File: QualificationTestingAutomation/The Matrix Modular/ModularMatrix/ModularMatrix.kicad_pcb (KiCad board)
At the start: 4 copper layers, 92.7 x 116.8 mm, 82 parts, among them J1 Conn_02x32_Counter_Clockwise_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, J2 Raspberry_Pi_2_3, J3 Barrel_Jack_MountingPin, J5 Conn_02x32_Counter_Clockwise_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, J6 Banana Jack, J7 Banana Jack, J8 Banana Jack, J9 Banana Jack, U1 TPS563210, U2 LT8361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

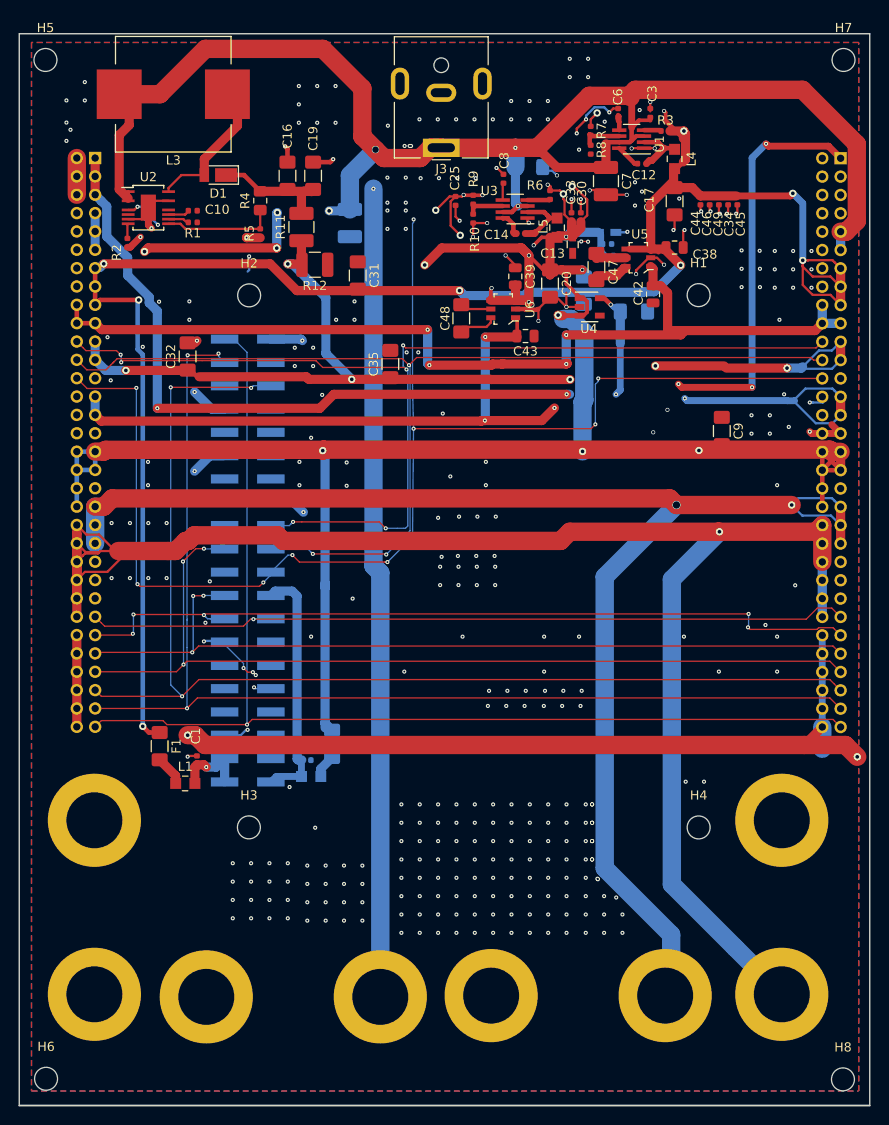
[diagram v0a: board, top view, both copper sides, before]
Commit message: Cleaned up the libraries Cleaned up the tracks Adjusted footprints to the manufacturers minimum size.
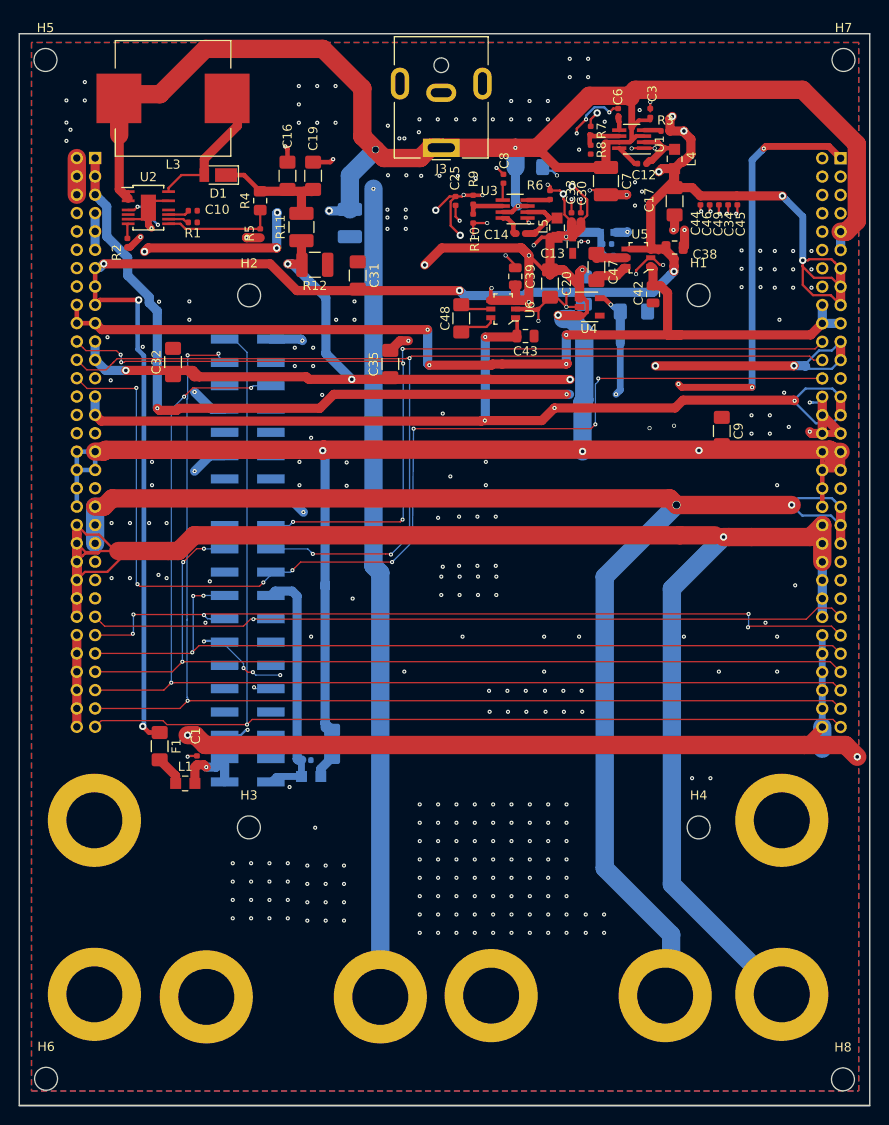
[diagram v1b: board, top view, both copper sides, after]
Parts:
- moved C32 1.70 mm to (178.0, 90.7)
- moved L3 0.46 mm to (178.0, 62.0)
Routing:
- net MOSI0: track 146.0 -> 122.8 mm, vias 9 -> 8
- net VD: track 223.1 -> 202.8 mm
- net SCLK1: track 128.0 -> 123.6 mm
- net GND: track 115.9 -> 119.3 mm, vias 346 -> 310
- net SCLK0: track 119.3 -> 116.5 mm
- net +5V: track 198.9 -> 196.4 mm, vias 10 -> 11
- net HT: track 115.0 -> 117.3 mm
- net +12V: track 202.3 -> 201.1 mm
- net MOSI1: track 125.5 -> 124.4 mm
- net -3V3: track 109.9 -> 108.9 mm
- net MISO0: track 117.8 -> 118.5 mm
- net +1V8: track 149.6 -> 149.0 mm

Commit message: Added Voltage and current measurment of the muxes and relays to the MSP Some clean up of the tracks.
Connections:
- J1 pad 49: GND -> VD
- J5 pad 49: GND -> VD
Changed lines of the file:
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@@
   )
   (setup
-    (last_trace_width 0.125)
+    (last_trace_width 0.0889)
     (user_trace_width 0.09)
     (user_trace_width 0.125)
@@
       (net 34 VD))
     (pad 49 thru_hole oval (at 0 -48 180) (size 1.35 1.35) (drill 0.8) (layers *.Cu *.Mask)
-      (net 1 GND))
+      (net 34 VD))
     (pad 48 thru_hole oval (at 2 -46 180) (size 1.35 1.35) (drill 0.8) (layers *.Cu *.Mask)
       (net 34 VD))
@@
       (net 34 VD))
     (pad 49 thru_hole oval (at 0 -48 180) (size 1.35 1.35) (drill 0.8) (layers *.Cu *.Mask)
-      (net 1 GND))
+      (net 34 VD))
     (pad 48 thru_hole oval (at 2 -46 180) (size 1.35 1.35) (drill 0.8) (layers *.Cu *.Mask)
       (net 34 VD))
@@
   (via (at 232.8672 106.299) (size 0.9) (drill 0.8) (layers F.Cu B.Cu) (net 33))
   (segment (start 233.0705 106.5023) (end 232.8672 106.299) (width 1) (layer F.Cu) (net 33))
-  (segment (start 188.707 118.51894) (end 188.707 118.383731) (width 0.09) (layer B.Cu) (net 37) (status 30))
-  (segment (start 183.6112 118.7018) (end 181.9862 118.7018) (width 0.125) (layer B.Cu) (net 38) (status 10))
-  (via (at 181.3052 116.1923) (size 0.45) (drill 0.2) (layers F.Cu B.Cu) (net 39))
-  (segment (start 183.6112 116.1618) (end 181.3357 116.1618) (width 0.125) (layer B.Cu) (net 39) (status 10))
-  (segment (start 181.3357 116.1618) (end 181.3052 116.1923) (width 0.125) (layer B.Cu) (net 39))
-  (via (at 180.1876 116.2177) (size 0.45) (drill 0.2) (layers F.Cu B.Cu) (net 39))
-  (segment (start 181.3052 116.1923) (end 180.213 116.1923) (width 0.125) (layer F.Cu) (net 39))
-  (segment (start 180.213 116.1923) (end 180.1876 116.2177) (width 0.125) (layer F.Cu) (net 39))
-  (segment (start 183.657 110.89894) (end 183.16956 110.89894) (width 0.5) (layer B.Cu) (net 40) (status 30))
-  (segment (start 183.6112 111.0818) (end 182.6112 111.0818) (width 0.125) (layer B.Cu) (net 40) (status 30))
-  (segment (start 183.657 105.81894) (end 183.20045 105.81894) (width 0.5) (layer B.Cu) (net 53) (status 30))
-  (segment (start 183.657 105.81894) (end 182.582 105.81894) (width 0.25) (layer B.Cu) (net 53) (status 30))
-  (segment (start 226.629065 64.537225) (end 226.455065 64.363225) (width 0.25) (layer F.Cu) (net 62))
-  (segment (start 226.629065 65.438225) (end 226.629065 64.537225) (width 0.25) (layer F.Cu) (net 62) (status 10))
-  (segment (start 226.5045 64.31379) (end 226.5045 63.7945) (width 0.0889) (layer F.Cu) (net 62) (status 30))
-  (segment (start 226.455065 64.363225) (end 226.5045 64.31379) (width 0.0889) (layer F.Cu) (net 62) (status 20))
-  (segment (start 226.5045 64.41266) (end 226.5045 64.1895) (width 0.5) (layer F.Cu) (net 62) (status 20))
-  (segment (start 226.629065 64.537225) (end 226.5045 64.41266) (width 0.5) (layer F.Cu) (net 62))
-  (segment (start 226.629065 63.919065) (end 226.5045 63.7945) (width 0.5) (layer F.Cu) (net 62) (status 30))
-  (segment (start 226.629065 65.438225) (end 226.629065 63.919065) (width 0.5) (layer F.Cu) (net 62) (status 30))
-  (segment (start 213.929065 71.301225) (end 214.009065 71.221225) (width 0.25) (layer F.Cu) (net 63) (status 30))
-  (segment (start 213.929065 73.058225) (end 213.929065 71.301225) (width 0.25) (layer F.Cu) (net 63) (status 30))
-  (segment (start 228.31884 69.088) (end 226.629065 67.398225) (width 0.5) (layer F.Cu) (net 64) (status 20))
-  (segment (start 228.623 69.088) (end 228.31884 69.088) (width 0.5) (layer F.Cu) (net 64) (status 10))
-  (segment (start 215.087065 75.695225) (end 214.438065 75.046225) (width 0.5) (layer F.Cu) (net 65) (status 20))
-  (segment (start 215.087065 76.570225) (end 215.087065 75.695225) (width 0.5) (layer F.Cu) (net 65))
-  (segment (start 213.957065 75.046225) (end 213.929065 75.018225) (width 0.5) (layer F.Cu) (net 65) (status 30))
-  (segment (start 214.438065 75.046225) (end 213.957065 75.046225) (width 0.5) (layer F.Cu) (net 65) (status 30))
-  (segment (start 215.22484 76.708) (end 215.087065 76.570225) (width 0.75) (layer F.Cu) (net 65) (status 10))
-  (segment (start 215.415 76.708) (end 215.22484 76.708) (width 0.75) (layer F.Cu) (net 65) (status 30))
   (via (at 245.4275 106.299) (size 0.8) (drill 0.4) (layers F.Cu B.Cu) (net 33))
   (segment (start 232.8672 106.299) (end 245.4275 106.299) (width 2) (layer F.Cu) (net 33))
@@
   (segment (start 251.2863 132.461) (end 252.575437 133.750137) (width 2) (layer F.Cu) (net 36))
   (segment (start 248.7615 130.5023) (end 248.7615 132.874) (width 2) (layer B.Cu) (net 36))
+  (segment (start 188.707 118.51894) (end 188.707 118.383731) (width 0.09) (layer B.Cu) (net 37) (status 30))
   (via (at 186.7535 118.745) (size 0.45) (drill 0.2) (layers F.Cu B.Cu) (net 37))
   (segment (start 188.6512 118.7018) (end 186.7967 118.7018) (width 0.125) (layer B.Cu) (net 37))
@@
   (segment (start 186.7535 118.745) (end 247.015 118.745) (width 0.125) (layer F.Cu) (net 37))
   (segment (start 247.015 118.745) (end 248.2215 117.5385) (width 0.125) (layer F.Cu) (net 37))
+  (segment (start 183.6112 118.7018) (end 181.9862 118.7018) (width 0.125) (layer B.Cu) (net 38) (status 10))
   (via (at 173.6725 118.237) (size 0.45) (drill 0.2) (layers F.Cu B.Cu) (net 38))
   (via (at 173.609 120.3325) (size 0.45) (drill 0.2) (layers F.Cu B.Cu) (net 38))
@@
   (segment (start 240.792 119.507) (end 249.7662 119.507) (width 0.125) (layer F.Cu) (net 38))
   (segment (start 240.665 119.634) (end 240.792 119.507) (width 0.125) (layer F.Cu) (net 38))
+  (via (at 181.3052 116.1923) (size 0.45) (drill 0.2) (layers F.Cu B.Cu) (net 39))
+  (segment (start 183.6112 116.1618) (end 181.3357 116.1618) (width 0.125) (layer B.Cu) (net 39) (status 10))
+  (segment (start 181.3357 116.1618) (end 181.3052 116.1923) (width 0.125) (layer B.Cu) (net 39))
+  (via (at 180.1876 116.2177) (size 0.45) (drill 0.2) (layers F.Cu B.Cu) (net 39))
+  (segment (start 181.3052 116.1923) (end 180.213 116.1923) (width 0.125) (layer F.Cu) (net 39))
+  (segment (start 180.213 116.1923) (end 180.1876 116.2177) (width 0.125) (layer F.Cu) (net 39))
   (via (at 180.086002 122.364498) (size 0.45) (drill 0.2) (layers F.Cu B.Cu) (net 39))
   (segment (start 180.1876 122.2629) (end 180.086002 122.364498) (width 0.125) (layer B.Cu) (net 39))
@@
   (segment (start 250.7615 122.5023) (end 249.890705 121.631505) (width 0.125) (layer F.Cu) (net 39))
   (segment (start 180.1876 116.2177) (end 180.1876 122.2629) (width 0.125) (layer B.Cu) (net 39))
+  (segment (start 183.657 110.89894) (end 183.16956 110.89894) (width 0.5) (layer B.Cu) (net 40) (status 30))
+  (segment (start 183.6112 111.0818) (end 182.6112 111.0818) (width 0.125) (layer B.Cu) (net 40) (status 30))
   (via (at 181.356 111.0615) (size 0.45) (drill 0.2) (layers F.Cu B.Cu) (net 40))
   (segment (start 183.6112 111.0818) (end 181.3763 111.0818) (width 0.125) (layer B.Cu) (net 40))
@@
   (segment (start 201.7395 111.6965) (end 201.67601 111.63301) (width 0.125) (layer F.Cu) (net 43))
   (segment (start 201.67601 111.63301) (end 201.16799 111.63301) (width 0.125) (layer F.Cu) (net 43))
+  (segment (start 183.657 105.81894) (end 183.20045 105.81894) (width 0.5) (layer B.Cu) (net 53) (status 30))
+  (segment (start 183.657 105.81894) (end 182.582 105.81894) (width 0.25) (layer B.Cu) (net 53) (status 30))
+  (segment (start 226.629065 64.537225) (end 226.455065 64.363225) (width 0.25) (layer F.Cu) (net 62))
+  (segment (start 226.629065 65.438225) (end 226.629065 64.537225) (width 0.25) (layer F.Cu) (net 62) (status 10))
+  (segment (start 226.5045 64.31379) (end 226.5045 63.7945) (width 0.0889) (layer F.Cu) (net 62) (status 30))
+  (segment (start 226.455065 64.363225) (end 226.5045 64.31379) (width 0.0889) (layer F.Cu) (net 62) (status 20))
+  (segment (start 226.5045 64.41266) (end 226.5045 64.1895) (width 0.5) (layer F.Cu) (net 62) (status 20))
+  (segment (start 226.629065 64.537225) (end 226.5045 64.41266) (width 0.5) (layer F.Cu) (net 62))
+  (segment (start 226.629065 63.919065) (end 226.5045 63.7945) (width 0.5) (layer F.Cu) (net 62) (status 30))
+  (segment (start 226.629065 65.438225) (end 226.629065 63.919065) (width 0.5) (layer F.Cu) (net 62) (status 30))
+  (segment (start 213.929065 71.301225) (end 214.009065 71.221225) (width 0.25) (layer F.Cu) (net 63) (status 30))
+  (segment (start 213.929065 73.058225) (end 213.929065 71.301225) (width 0.25) (layer F.Cu) (net 63) (status 30))
+  (segment (start 228.31884 69.088) (end 226.629065 67.398225) (width 0.5) (layer F.Cu) (net 64) (status 20))
+  (segment (start 228.623 69.088) (end 228.31884 69.088) (width 0.5) (layer F.Cu) (net 64) (status 10))
+  (segment (start 215.087065 75.695225) (end 214.438065 75.046225) (width 0.5) (layer F.Cu) (net 65) (status 20))
+  (segment (start 215.087065 76.570225) (end 215.087065 75.695225) (width 0.5) (layer F.Cu) (net 65))
+  (segment (start 213.957065 75.046225) (end 213.929065 75.018225) (width 0.5) (layer F.Cu) (net 65) (status 30))
+  (segment (start 214.438065 75.046225) (end 213.957065 75.046225) (width 0.5) (layer F.Cu) (net 65) (status 30))
+  (segment (start 215.22484 76.708) (end 215.087065 76.570225) (width 0.75) (layer F.Cu) (net 65) (status 10))
+  (segment (start 215.415 76.708) (end 215.22484 76.708) (width 0.75) (layer F.Cu) (net 65) (status 30))
   (via (at 186.4995 93.5355) (size 0.45) (drill 0.2) (layers F.Cu B.Cu) (net 68))
   (segment (start 186.7332 93.3018) (end 188.6512 93.3018) (width 0.125) (layer B.Cu) (net 68))
